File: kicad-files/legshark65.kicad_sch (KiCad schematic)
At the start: 158 parts, among them J1 ARM JTAG, SW1 K2-1187SQ-A4SW-06, SW2 PCM12SMTR, T2 53261-0471, U1 STM32F411CEU6, U3 AT24C256C-SSHL-T, Y1 TAXM8M4RFDCET2T

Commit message: More minor clearance changes
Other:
- moved on the sheet: C11
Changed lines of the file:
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@@
   (junction (at 356.235 147.955) (diameter 0) (color 0 0 0 0)
   )
-  (junction (at 205.74 312.42) (diameter 0) (color 0 0 0 0)
-  )
   (junction (at 102.235 71.755) (diameter 0) (color 0 0 0 0)
   )
@@
   (junction (at 240.665 85.725) (diameter 0) (color 0 0 0 0)
   )
+  (junction (at 198.12 321.31) (diameter 0) (color 0 0 0 0)
+  )
   (junction (at 189.865 111.125) (diameter 0) (color 0 0 0 0)
   )
@@
   (junction (at 280.035 97.155) (diameter 0) (color 0 0 0 0)
   )
+  (junction (at 205.74 321.31) (diameter 0) (color 0 0 0 0)
+  )
   (junction (at 88.265 85.725) (diameter 0) (color 0 0 0 0)
   )
@@
   (junction (at 105.41 255.27) (diameter 0) (color 0 0 0 0)
   )
-  (junction (at 199.39 308.61) (diameter 0) (color 0 0 0 0)
-  )
   (junction (at 102.235 97.155) (diameter 0) (color 0 0 0 0)
   )
@@
     (stroke (width 0) (type default))
   )
-  (wire (pts (xy 127 267.335) (xy 127 265.43))
-    (stroke (width 0) (type default))
-  )
   (wire (pts (xy 81.915 85.725) (xy 88.265 85.725))
     (stroke (width 0) (type default))
@@
     (stroke (width 0) (type default))
   )
-  (wire (pts (xy 199.39 306.07) (xy 199.39 308.61))
-    (stroke (width 0) (type default))
-  )
   (wire (pts (xy 280.035 116.205) (xy 280.035 117.475))
     (stroke (width 0) (type default))
@@
     (stroke (width 0) (type default))
   )
-  (wire (pts (xy 205.74 312.42) (xy 205.74 306.07))
+  (wire (pts (xy 205.74 306.07) (xy 205.74 321.31))
     (stroke (width 0) (type default))
   )
@@
     (stroke (width 0) (type default))
   )
-  (wire (pts (xy 208.28 312.42) (xy 205.74 312.42))
-    (stroke (width 0) (type default))
-  )
   (wire (pts (xy 381.635 40.005) (xy 381.635 41.275))
     (stroke (width 0) (type default))
@@
     (stroke (width 0) (type default))
   )
+  (wire (pts (xy 198.12 325.755) (xy 198.12 321.31))
+    (stroke (width 0) (type default))
+  )
   (wire (pts (xy 102.235 65.405) (xy 102.235 66.675))
     (stroke (width 0) (type default))
@@
     (stroke (width 0) (type default))
   )
+  (wire (pts (xy 205.74 324.485) (xy 205.74 321.31))
+    (stroke (width 0) (type default))
+  )
   (wire (pts (xy 109.22 246.38) (xy 93.98 246.38))
     (stroke (width 0) (type default))
@@
     (stroke (width 0) (type default))
   )
-  (wire (pts (xy 205.74 318.77) (xy 205.74 312.42))
-    (stroke (width 0) (type default))
-  )
   (wire (pts (xy 203.835 122.555) (xy 229.235 122.555))
     (stroke (width 0) (type default))
   )
-  (wire (pts (xy 123.19 267.335) (xy 127 267.335))
+  (wire (pts (xy 121.92 265.43) (xy 127 265.43))
     (stroke (width 0) (type default))
   )
@@
     (stroke (width 0) (type default))
   )
-  (wire (pts (xy 199.39 311.15) (xy 199.39 308.61))
+  (wire (pts (xy 199.39 306.07) (xy 199.39 316.865))
     (stroke (width 0) (type default))
   )
@@
     (stroke (width 0) (type default))
   )
+  (wire (pts (xy 199.39 316.865) (xy 198.12 316.865))
+    (stroke (width 0) (type default))
+  )
   (wire (pts (xy 127 224.155) (xy 127 227.33))
     (stroke (width 0) (type default))
@@
     (stroke (width 0) (type default))
   )
+  (wire (pts (xy 198.12 316.865) (xy 198.12 321.31))
+    (stroke (width 0) (type default))
+  )
   (wire (pts (xy 229.235 40.005) (xy 229.235 41.275))
     (stroke (width 0) (type default))
@@
     (stroke (width 0) (type default))
   )
-  (wire (pts (xy 205.74 318.77) (xy 199.39 318.77))
-    (stroke (width 0) (type default))
-  )
   (wire (pts (xy 143.51 210.82) (xy 143.51 213.36))
     (stroke (width 0) (type default))
@@
     )
   )
-  (global_label "3V3" (shape input) (at 208.28 312.42 0) (fields_autoplaced)
-    (effects (font (size 1.27 1.27)) (justify left))
-    (property "Intersheetrefs" "${INTERSHEET_REFS}" (at 214.0392 312.42 0)
-      (effects (font (size 1.27 1.27)) (justify left) hide)
+  (global_label "3V3" (shape input) (at 205.74 324.485 270) (fields_autoplaced)
+    (effects (font (size 1.27 1.27)) (justify right))
+    (property "Intersheetrefs" "${INTERSHEET_REFS}" (at 205.74 330.2442 90)
+      (effects (font (size 1.27 1.27)) (justify right) hide)
     )
   )
@@
     )
   )
-  (global_label "NRST" (shape input) (at 123.19 267.335 180) (fields_autoplaced)
+  (global_label "NRST" (shape input) (at 121.92 265.43 180) (fields_autoplaced)
     (effects (font (size 1.27 1.27)) (justify right))
-    (property "Intersheetrefs" "${INTERSHEET_REFS}" (at 116.1608 267.335 0)
+    (property "Intersheetrefs" "${INTERSHEET_REFS}" (at 114.8908 265.43 0)
       (effects (font (size 1.27 1.27)) (justify right) hide)
     )
@@
     )
   )
-  (symbol (lib_id "power:GND") (at 199.39 308.61 90) (unit 1)
+  (symbol (lib_id "power:GND") (at 198.12 325.755 0) (unit 1)
     (in_bom yes) (on_board yes) (dnp no)
-    (property "Reference" "#PWR029" (at 205.74 308.61 0)
+    (property "Reference" "#PWR029" (at 198.12 332.105 0)
       (effects (font (size 1.27 1.27)) hide)
     )
-    (property "Value" "GND" (at 203.2 308.61 0)
+    (property "Value" "GND" (at 198.12 329.565 0)
       (effects (font (size 1.27 1.27)))
     )
-    (property "Footprint" "" (at 199.39 308.61 0)
+    (property "Footprint" "" (at 198.12 325.755 0)
       (effects (font (size 1.27 1.27)) hide)
     )
-    (property "Datasheet" "" (at 199.39 308.61 0)
+    (property "Datasheet" "" (at 198.12 325.755 0)
       (effects (font (size 1.27 1.27)) hide)
     )
@@
     )
   )
-  (symbol (lib_id "Device:C") (at 199.39 314.96 0) (unit 1)
+  (symbol (lib_id "Device:C") (at 201.93 321.31 90) (unit 1)
     (in_bom yes) (on_board yes) (dnp no)
-    (property "Reference" "C11" (at 201.93 314.96 0)
+    (property "Reference" "C11" (at 201.93 318.77 0)
       (effects (font (size 1.27 1.27)) (justify left))
     )
-    (property "Value" "100n" (at 201.93 317.5 0)
+    (property "Value" "100n" (at 204.47 318.77 0)
       (effects (font (size 1.27 1.27)) (justify left))
     )
-    (property "Footprint" "Capacitor_SMD:C_0603_1608Metric_Pad1.08x0.95mm_HandSolder" (at 200.3552 318.77 0)
+    (property "Footprint" "Capacitor_SMD:C_0603_1608Metric_Pad1.08x0.95mm_HandSolder" (at 205.74 320.3448 0)
       (effects (font (size 1.27 1.27)) hide)
     )
-    (property "Datasheet" "~" (at 199.39 314.96 0)
+    (property "Datasheet" "~" (at 201.93 321.31 0)
       (effects (font (size 1.27 1.27)) hide)
     )

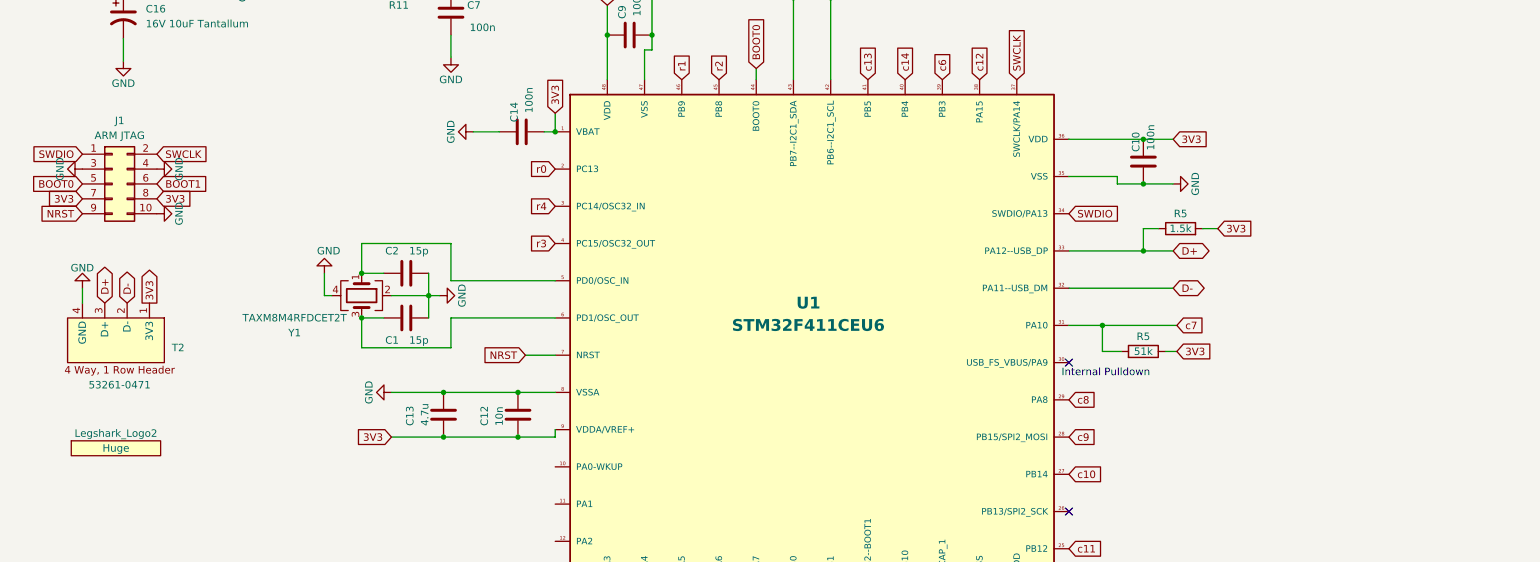
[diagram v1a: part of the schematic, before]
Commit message: Added some front graphics to the motherboard pcb
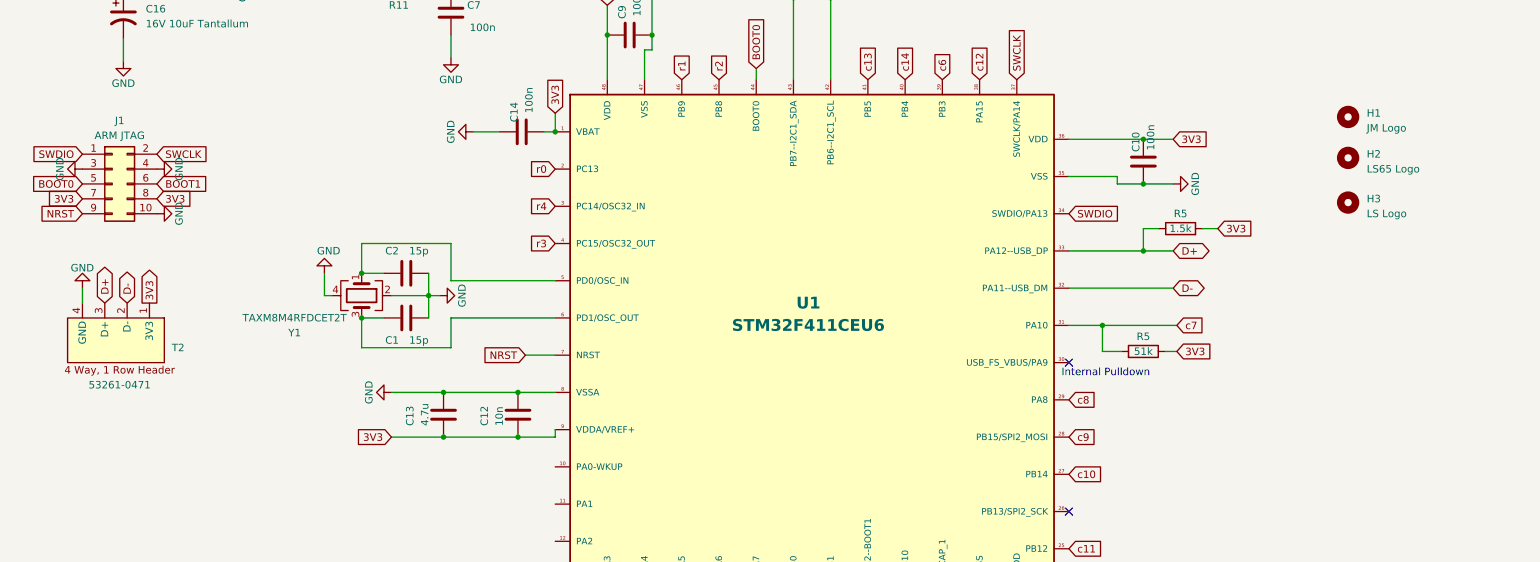
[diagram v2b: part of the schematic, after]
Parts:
- removed Legshark_Logo2: Huge, Legshark:Legshark_Logo_Huge, symbol legshark_symbols:Legshark_Logo
- added H1: JM Logo, Legshark:jm_logo, symbol Mechanical:MountingHole
- added H2: LS65 Logo, Legshark:ls65_logo, symbol Mechanical:MountingHole
- added H3: LS Logo, Legshark:Legshark_Mask, symbol Mechanical:MountingHole
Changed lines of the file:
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@@
+    )
+  )
+  (symbol (lib_id "Mechanical:MountingHole") (at 262.255 239.395 0) (unit 1)
+    (in_bom yes) (on_board yes) (dnp no) (fields_autoplaced)
+    (property "Reference" "H3" (at 265.43 238.76 0)
+      (effects (font (size 1.27 1.27)) (justify left))
+    )
+    (property "Value" "LS Logo" (at 265.43 241.3 0)
+      (effects (font (size 1.27 1.27)) (justify left))
+    )
+    (property "Footprint" "Legshark:Legshark_Mask" (at 262.255 239.395 0)
+      (effects (font (size 1.27 1.27)) hide)
+    )
+    (property "Datasheet" "~" (at 262.255 239.395 0)
+      (effects (font (size 1.27 1.27)) hide)
+    )
+    (instances
+      (project "legshark65"
+        (path "/9ddf6dc5-8b5e-413a-9b25-d1d5a5a60469"
+          (reference "H3") (unit 1)
+        )
+      )
     )
   )
@@
         (path "/9ddf6dc5-8b5e-413a-9b25-d1d5a5a60469"
           (reference "R15") (unit 1)
+        )
+      )
+    )
+  )
+  (symbol (lib_id "Mechanical:MountingHole") (at 262.255 224.79 0) (unit 1)
+    (in_bom yes) (on_board yes) (dnp no) (fields_autoplaced)
+    (property "Reference" "H1" (at 265.43 224.155 0)
+      (effects (font (size 1.27 1.27)) (justify left))
+    )
+    (property "Value" "JM Logo" (at 265.43 226.695 0)
+      (effects (font (size 1.27 1.27)) (justify left))
+    )
+    (property "Footprint" "Legshark:jm_logo" (at 262.255 224.79 0)
+      (effects (font (size 1.27 1.27)) hide)
+    )
+    (property "Datasheet" "~" (at 262.255 224.79 0)
+      (effects (font (size 1.27 1.27)) hide)
+    )
+    (instances
+      (project "legshark65"
+        (path "/9ddf6dc5-8b5e-413a-9b25-d1d5a5a60469"
+          (reference "H1") (unit 1)
         )
       )
@@
     )
   )
+  (symbol (lib_id "Mechanical:MountingHole") (at 262.255 231.775 0) (unit 1)
+    (in_bom yes) (on_board yes) (dnp no) (fields_autoplaced)
+    (property "Reference" "H2" (at 265.43 231.14 0)
+      (effects (font (size 1.27 1.27)) (justify left))
+    )
+    (property "Value" "LS65 Logo" (at 265.43 233.68 0)
+      (effects (font (size 1.27 1.27)) (justify left))
+    )
+    (property "Footprint" "Legshark:ls65_logo" (at 262.255 231.775 0)
+      (effects (font (size 1.27 1.27)) hide)
+    )
+    (property "Datasheet" "~" (at 262.255 231.775 0)
+      (effects (font (size 1.27 1.27)) hide)
+    )
+    (instances
+      (project "legshark65"
+        (path "/9ddf6dc5-8b5e-413a-9b25-d1d5a5a60469"
+          (reference "H2") (unit 1)
+        )
+      )
+    )
+  )
   (symbol (lib_id "MX_Alps_Hybrid:MX-NoLED") (at 52.705 137.795 0) (unit 1)
     (in_bom yes) (on_board yes) (dnp no)
@@
         )
       )
-    )
-  )
-  (symbol (lib_id "legshark_symbols:Legshark_Logo") (at 52.07 281.305 0) (unit 1)
-    (in_bom yes) (on_board yes) (dnp no)
-    (property "Reference" "Legshark_Logo2" (at 52.07 278.765 0)
-      (effects (font (size 1.27 1.27)))
-    )
-    (property "Value" "Huge" (at 52.07 281.305 0)
-      (effects (font (size 1.27 1.27)))
-    )
-    (property "Footprint" "Legshark:Legshark_Logo_Huge" (at 52.07 281.305 0)
-      (effects (font (size 1.27 1.27)) hide)
-    )
-    (property "Datasheet" "" (at 52.07 281.305 0)
-      (effects (font (size 1.27 1.27)) hide)
-    )
-    (instances
-      (project "old_layout"
-        (path "/2fda2561-53ed-4930-8b41-858e0e3dd5f4"
-          (reference "Legshark_Logo2") (unit 1)
-        )
-      )
-      (project "legshark65"
-        (path "/9ddf6dc5-8b5e-413a-9b25-d1d5a5a60469"
-          (reference "Legshark_Logo2") (unit 1)
-        )
-      )

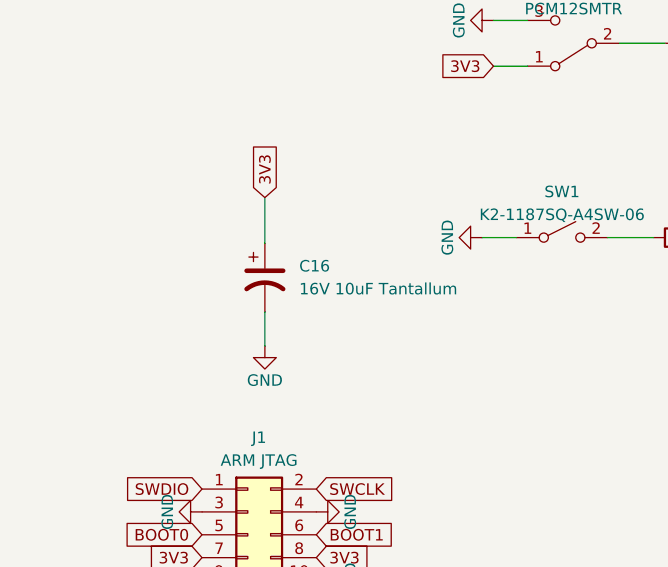
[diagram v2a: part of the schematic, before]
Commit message: Filling out the BOM of the motherboard
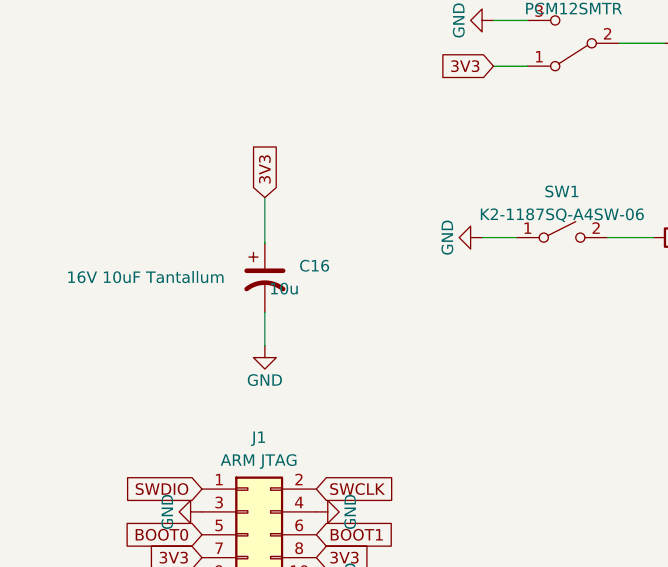
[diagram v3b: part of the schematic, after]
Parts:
- C1, C2: LCSC Part (none) -> C107037; Manufacturer (none) -> YAGEO; Manufacturer Part Number (none) -> CC0603JRNPO9BN150; Package (none) -> 0603; Specification (none) -> 50V 15pF NP0 ±5% 0603 Multilayer Ceramic Capacitors MLCC; Vendor Part Number (none) -> LCSC C107037
- C10, C11, C14, C17, C6, C7, C9: LCSC Part (none) -> C1591; Manufacturer (none) -> Samsung; Manufacturer Part Number (none) -> CL10B104KB8NNNC; Package (none) -> 0603; Specification (none) -> 50V 100nF X7R ±10% 0603 Multilayer Ceramic Capacitors MLCC; Vendor Part Number (none) -> LCSC C1591
- C12: LCSC Part (none) -> C1589; Manufacturer (none) -> Samsung; Manufacturer Part Number (none) -> CL10B103KB8NNNC; Package (none) -> 0603; Specification (none) -> 50V 10nF X7R ±10% 0603 Multilayer Ceramic Capacitors MLCC; Vendor Part Number (none) -> LCSC C1589
- C13, C15: LCSC Part (none) -> C2857987; Manufacturer (none) -> Guangdong Fenghua Advanced Tech; Manufacturer Part Number (none) -> 0603X475M100NT; Package (none) -> 0603; Specification (none) -> 10V 4.7uF ±20% 0603 Multilayer Ceramic Capacitors MLCC; Vendor Part Number (none) -> LCSC C2857987
- C16: value 16V 10uF Tantallum -> 10u; LCSC Part (none) -> C7171; Manufacturer (none) -> AVX; Manufacturer Part Number (none) -> TAJA106K016RNJ; Package (none) -> C3216 (CASE A); Specification (none) -> 16V 10uF Tantallum; Vendor Part Number (none) -> LCSC C7171
- D_0, D_1, D_10, D_11, D_12, D_13, D_14, D_15, D_16, D_17, D_18, D_19, D_2, D_20, D_21, D_22, D_23, D_24, D_25, D_26, D_27, D_28, D_29, D_3, D_30, D_31, D_32, D_33, D_34, D_35, D_36, D_37, D_38, D_39, D_4, D_40, D_41, D_42, D_43, D_44, D_45, D_46, D_47, D_48, D_49, D_5, D_50, D_51, D_52, D_53, D_54, D_55, D_56, D_57, D_58, D_59, D_6, D_60, D_61, D_62, D_63, D_64, D_7, D_8, D_9: LCSC Part (none) -> C81598; Manufacturer (none) -> Semtech; Manufacturer Part Number (none) -> 1N4148W; Package (none) -> SOD-123; Specification (none) -> Small-signal switching diodes; Vendor Part Number (none) -> LCSC C81598
- SW1: Manufacturer (none) -> Korean Hroparts; Manufacturer Part Number (none) -> K2-1187SQ-A4SW-06; Package (none) -> 5.0x5.0mm; Specification (none) -> 5.2mm 1.5mm Round Button SPST; Vendor Part Number (none) -> LCSC C92584
- SW2: LCSC Part (none) -> C221841; Manufacturer (none) -> C&K; Package (none) -> SMD; Specification (none) -> SPDT 6V SMD Slide Switches ROHS; Vendor Part Number (none) -> C221841
- U1: Manufacturer (none) -> STMicroelectronics; Manufacturer Part Number (none) -> STM32F411; Package (none) -> UFQFPN-48; Part Number STM32F411 -> (none); Vendor Part Number (none) -> LCSC C60420 (https://lcsc.com/product-detail/ST-Microelectr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
- U3: footprint acheron_Components:TSSOP-8_4.4x3mm_P0.65mm -> acheron_Components:SOIC-8; Manufacturer (none) -> Microchip; Manufacturer Part Number (none) -> AT24C256C-SSHL-T; Package (none) -> SOIC-8; Specification (none) -> SOIC-8 non-volatile 256Kb (32K x 8) I2C EEPROM; Vendor Part Number (none) -> LCSC C6482
- Y1: Manufacturer (none) -> TAE; Manufacturer Part Number (none) -> TAXM8M4RFDCET2T; Package (none) -> Y3225_4P; Specification (none) -> 8MHz 3225-4P oscillator crystal; Vendor Part Number (none) -> LCSC C403948
